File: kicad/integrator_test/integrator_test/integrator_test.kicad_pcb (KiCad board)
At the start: 2 copper layers, 52.3 x 48.3 mm, 35 parts, among them J1 Conn_01x03_Pin, J2 Conn_01x02_Pin, J3 Conn_01x04_Pin, J4 Conn_01x04_Pin, J5 Conn_01x06_Pin, SW1 SW_SPDT, U1 OPA189, U2 OPA189, U3 DG419DY-T1-E3, U4 MCP45HV51-ST, U5 DG408DQ-T1-E3

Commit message: integrator test board v2
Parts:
- removed C10: 100nF, Capacitor_SMD:C_0805_2012Metric
- removed the J1 at (61.5, 42.7)
- removed the J2 at (48.5, 48.5)
- removed J5: Conn_01x06_Pin, Connector_PinHeader_2.54mm:PinHeader_1x06_P2.54mm_Vertical
- removed R10, R7, R8, R9: 10M, Resistor_SMD:R_0603_1608Metric
- removed the R5 at (39.4, 47.8)
- removed the U4 at (39.9, 43.9)
- added J3: Conn_01x08_Pin, Connector_PinHeader_2.54mm:PinHeader_1x08_P2.54mm_Vertical, F.Cu at (20.6, 43.4)
- added U5: AD5290, Package_SO:MSOP-10_3x3mm_P0.5mm, F.Cu at (36.0, 28.7)
- C1, C11, C12, C13, C14, C2, C3, C4, C5, C6, C7, C8: footprint Capacitor_SMD:C_0805_2012Metric -> Capacitor_SMD:C_0603_1608Metric
- C9: value 100nF -> DNP; footprint Capacitor_SMD:C_0805_2012Metric -> Capacitor_SMD:C_0603_1608Metric
- moved J1 33.0 mm to (47.6, 38.2)
- moved C1 29.4 mm to (33.3, 40.3), turned to 0 degrees
- moved C6 28.5 mm to (37.5, 31.6)
- moved C2 27.8 mm to (33.3, 38.8), turned to 0 degrees
- moved C12 27.3 mm to (30.2, 38.1), turned to 180 degrees
- moved U2 24.8 mm to (35.6, 35.2)
- moved R6 23.7 mm to (40.7, 27.5)
- moved C13 22.0 mm to (31.1, 28.7), turned to 180 degrees
- moved C3 21.9 mm to (36.5, 40.3)
- moved C4 20.5 mm to (36.5, 38.8)
- moved C9 18.8 mm to (38.9, 39.6), turned to -90 degrees
- moved C11 18.3 mm to (44.5, 33.8)
- moved C5 17.4 mm to (51.3, 28.4), turned to 90 degrees
- moved R3 17.2 mm to (40.9, 32.9)
- moved SW1 16.6 mm to (33.5, 18.9), turned to 90 degrees
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- renumbered J3 to J1, J4 to J2, R1 to R2, R2 to R3, R3 to R4, R4 to R5, U3 to U1, U5 to U3, U1 to U4
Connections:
- C1 pad 1: I_OUT -> INT_R-
- C2 pad 1: I_OUT -> INT_R-
- C3 pad 1: I_OUT -> INT_R-
- C4 pad 1: I_OUT -> INT_R-
- C9 pad 1: +3V3 -> INT_R-
- C9 pad 2: GND -> I_OUT
- J2 pad 1: I_IN -> I_OUT
- J2 pad 4: I_OUT -> I_IN
- R6 pad 1: Net-(J1-Pin_1) -> INT_R+
- U3 pad 8: INT_R- -> I_OUT
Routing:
- net I_OUT: track 113.2 -> 36.2 mm, vias 0 -> 1
- net +12V: track 111.3 -> 47.0 mm, vias 4 -> 3
- net +3V3: track 52.2 -> 9.41 mm, vias 2 -> 0
- net INT_R-: track 62.4 -> 26.1 mm
- net I_OVERRIDE_EN: track 44.0 -> 77.3 mm, vias 0 -> 1
- net INT_R+: track 66.6 -> 33.4 mm
- net R_CLK: track 0.00 -> 32.4 mm, vias 0 -> 2
- net R_SDI: track 0.00 -> 30.7 mm, vias 0 -> 2
- net R_SDO: track 0.00 -> 28.8 mm, vias 0 -> 2
- net R_CS: track 0.00 -> 22.2 mm, vias 0 -> 2
- net Net-(SW1-C): track 45.7 -> 24.1 mm, vias 2 -> 0
- net -12V: track 106.1 -> 84.8 mm
- net I_OVERRIDE: track 46.4 -> 26.7 mm, vias 0 -> 2
- net R_SDA: track 19.2 -> 0.00 mm
- net R_SCL: track 18.7 -> 0.00 mm
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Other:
- board size 52.3 x 48.3 mm -> 36.6 x 47.2 mm

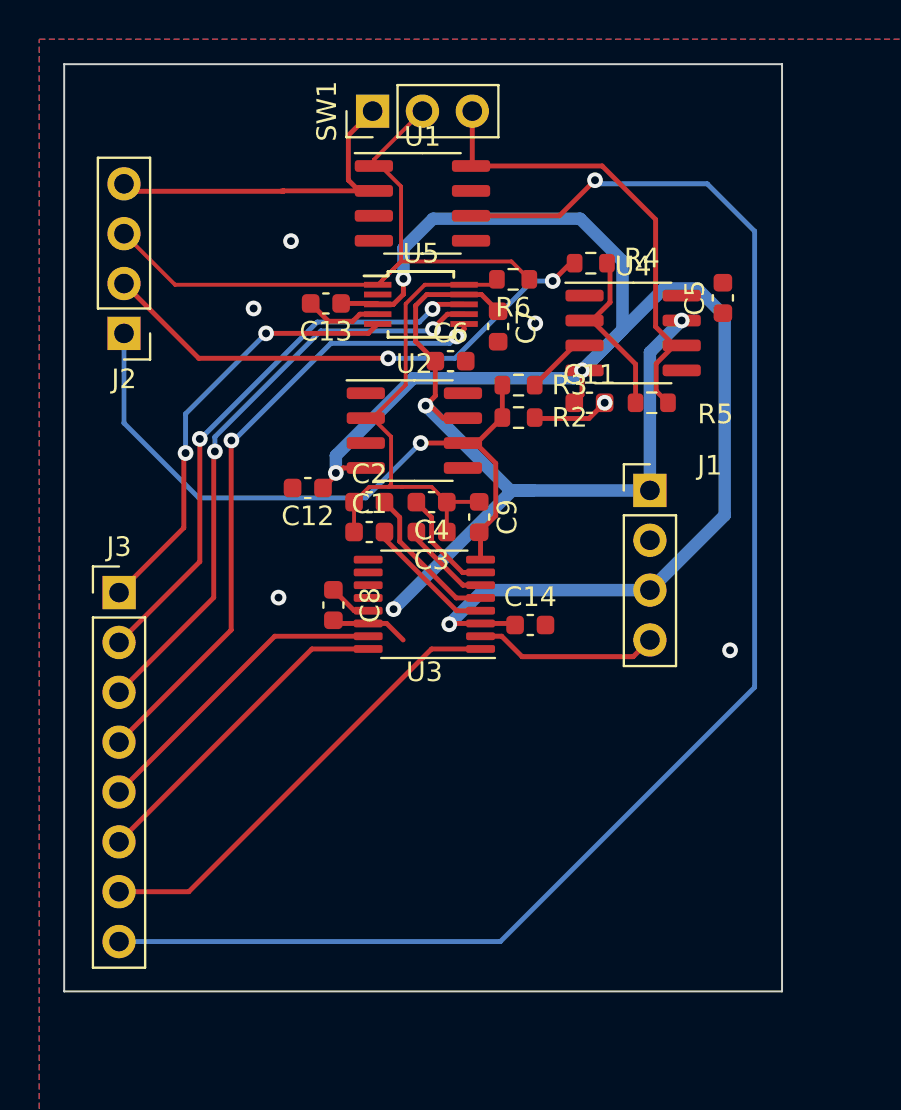
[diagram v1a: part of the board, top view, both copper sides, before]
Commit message: Optimzied some traces for the integrator test board
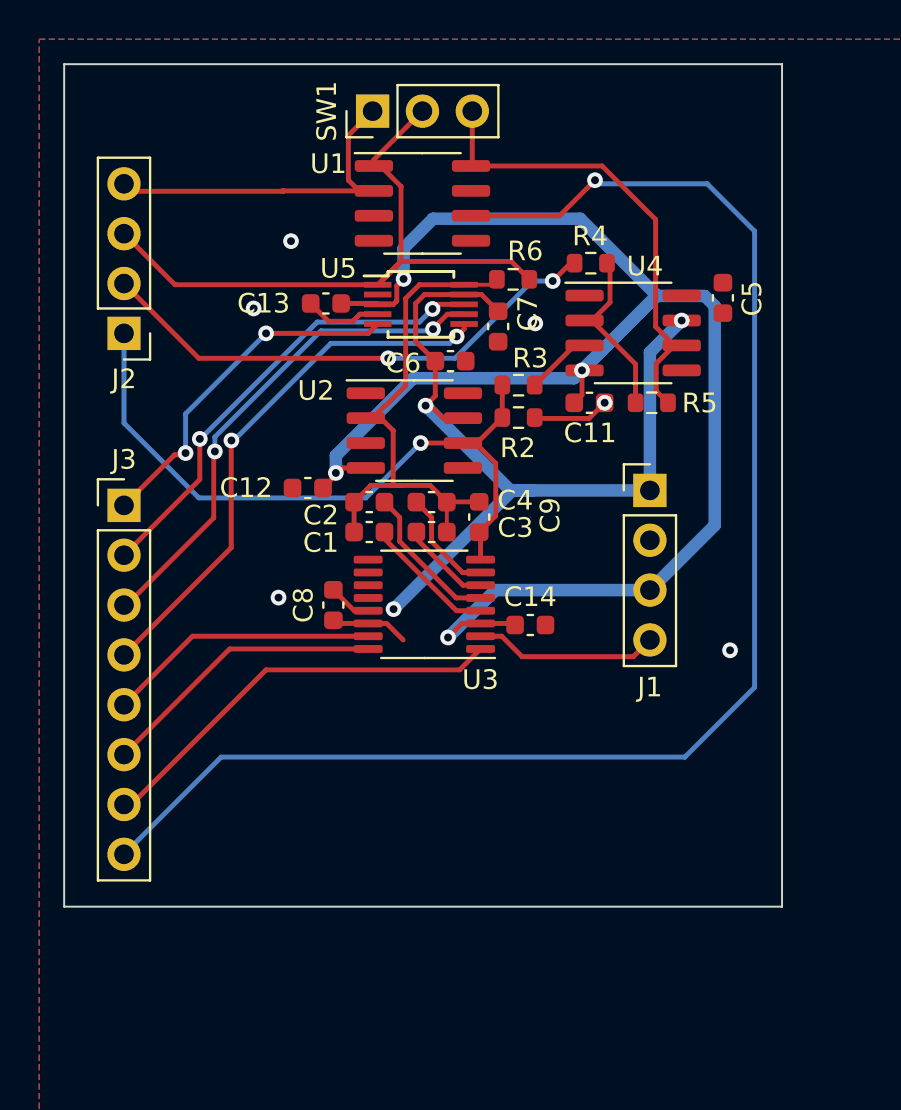
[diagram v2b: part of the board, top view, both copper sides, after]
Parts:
- moved J3 4.45 mm to (20.8, 39.0)
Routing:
- net R_CLK: track 32.4 -> 27.9 mm
- net R_SDO: track 28.8 -> 24.3 mm
- net R_SDI: track 30.7 -> 26.2 mm
- net R_CS: track 22.2 -> 17.9 mm
- net I_OVERRIDE_EN: track 77.3 -> 75.2 mm
- net INT_CAP_SEL_A2: track 16.0 -> 13.9 mm
- net INT_CAP_SEL_A1: track 16.8 -> 14.7 mm
- net INT_CAP_SEL_A0: track 23.5 -> 21.4 mm
- net -12V: track 84.8 -> 86.2 mm
- net INT_R-: track 26.1 -> 27.2 mm
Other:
- board size 36.6 x 47.2 mm -> 36.6 x 42.9 mm
